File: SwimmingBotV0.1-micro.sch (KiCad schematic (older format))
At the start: 32 parts, among them P11 DEBUG, U8 MAX6034_25, U9 STM32F446-144, X1 CRYSTAL_SMD, Y1 Crystal

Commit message: woohoo getting there
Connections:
- net PB7 is gone; now on net SDA: U9.137 (PB7)
- net PD3 is gone; now on net DCMI_D5: U9.117 (PD3)
- net DCMI_D5: no longer U9.136 (PB6)
- net SCL: now also U9.136 (PB6); no longer U9.69 (PB10)
- net SDA: no longer U9.70 (PB11)
- new net PB10: U9.69 (PB10)
- new net PB11: U9.70 (PB11)
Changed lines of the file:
@@
 $Descr A4 11693 8268
 encoding utf-8
-Sheet 8 8
+Sheet 7 8
 Title ""
 Date ""
@@
 Text HLabel 7050 1300 1    60   Input ~ 0
 DCMI_D4
-Text HLabel 4650 1300 1    60   Input ~ 0
+Text HLabel 6550 1300 1    60   Input ~ 0
 DCMI_D5
 Text HLabel 4350 1300 1    60   Input ~ 0
@@
 Wire Wire Line
 	4050 1350 4050 1300
-Text Label 7050 5800 3    60   ~ 0
+Text Label 4650 1300 1    60   ~ 0
 SCL
-Text Label 7150 5800 3    60   ~ 0
+Text Label 4550 1300 1    60   ~ 0
 SDA
 $Comp
@@
 Text HLabel 6950 1300 1    60   Input ~ 0
 PC12
-Text HLabel 6550 1300 1    60   Input ~ 0
-PD3
+Text HLabel 7150 5800 3    60   Input ~ 0
+PB11
 Text HLabel 5650 1300 1    60   Input ~ 0
 PG11
@@
 Text HLabel 5350 1300 1    60   Input ~ 0
 PG14
-Text HLabel 4550 1300 1    60   Input ~ 0
-PB7
+Text HLabel 7050 5800 3    60   Input ~ 0
+PB10
 $Comp
 L JUMPER JP1

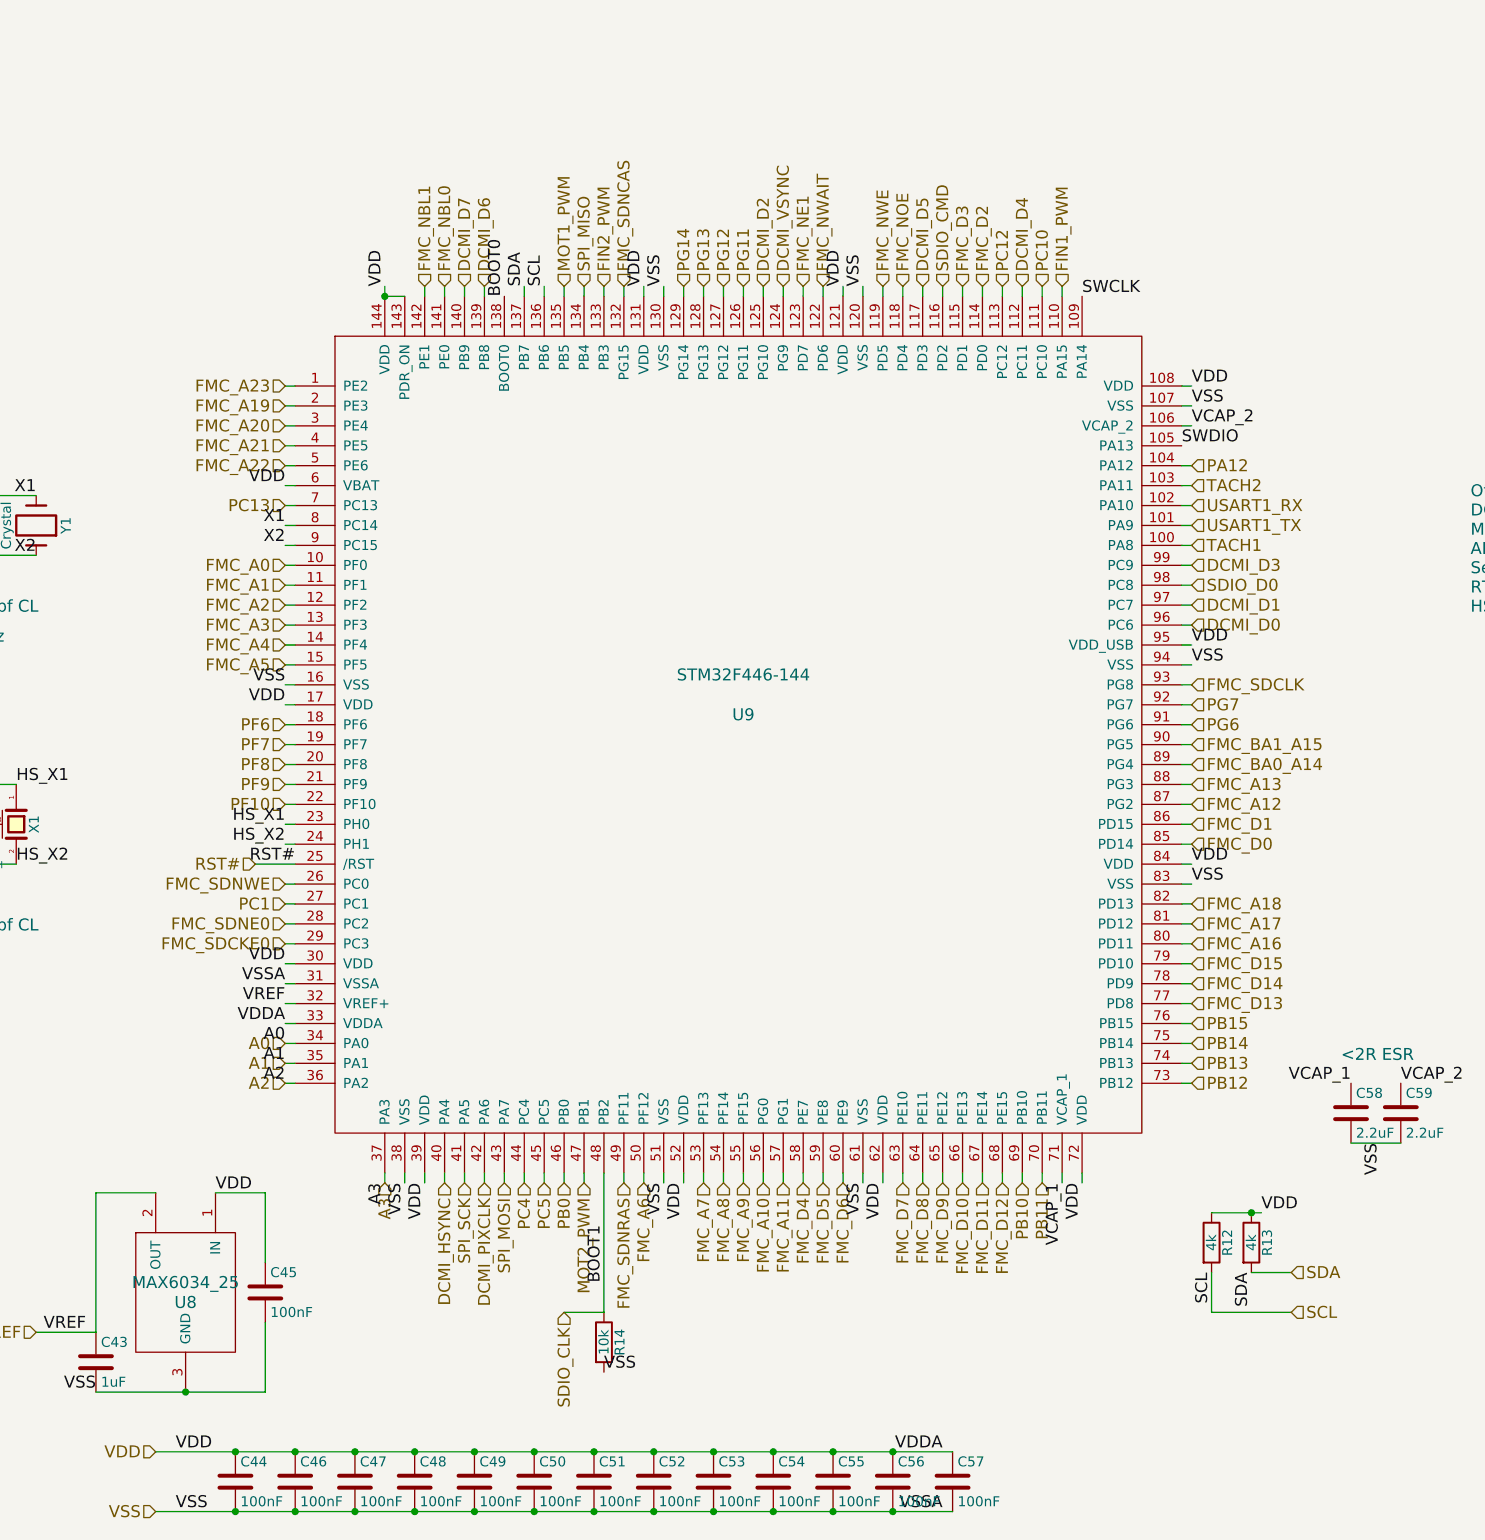
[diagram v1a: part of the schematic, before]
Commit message: removed old ram and flash, added new flash, switched to 100 pin micro
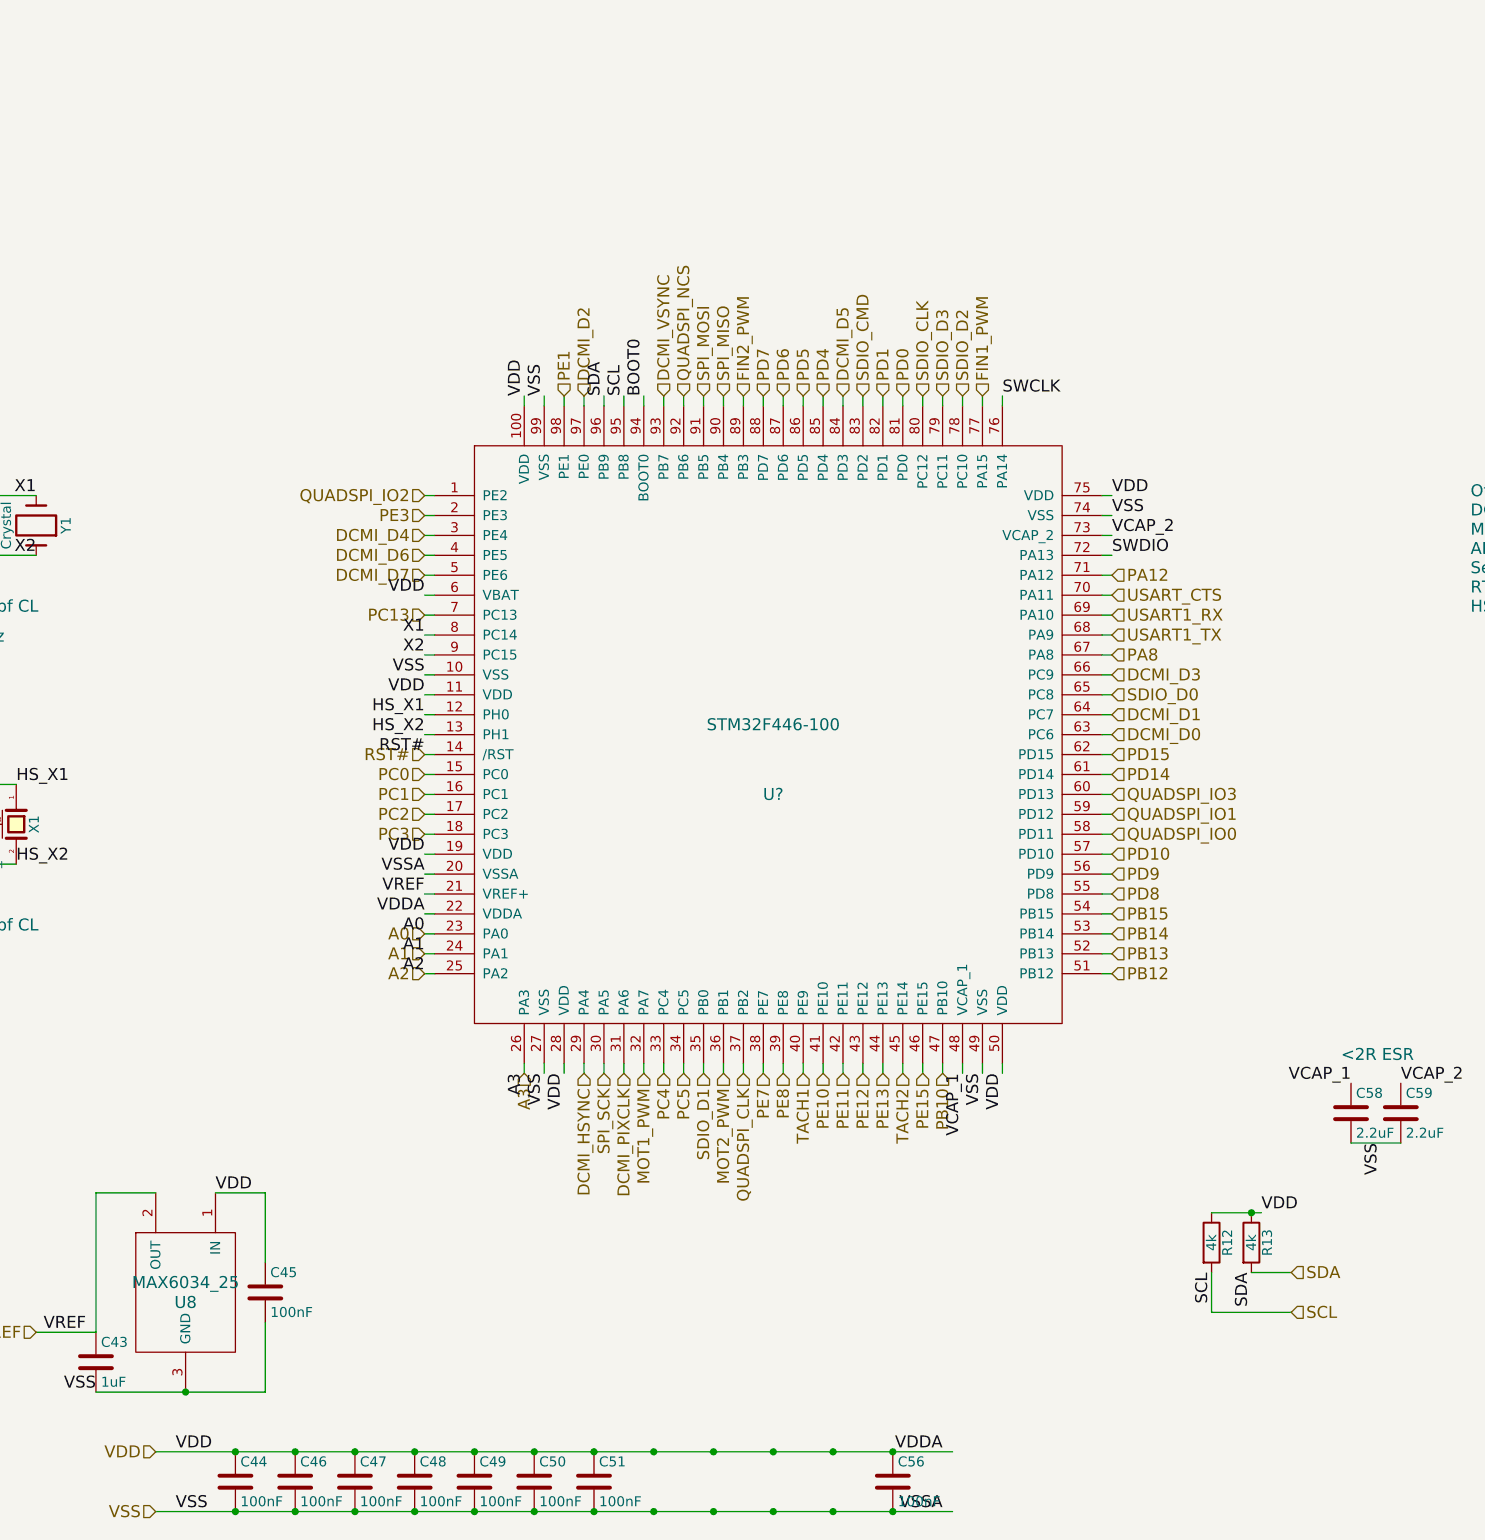
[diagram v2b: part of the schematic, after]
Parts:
- removed C52, C53, C54, C55, C57: 100nF, Capacitors_SMD:C_0402, symbol C
- removed R14: 10k, Resistors_SMD:R_0402, symbol R
- removed U9: STM32F446-144, Housings_QFP:LQFP-144_20x20mm_Pitch0.5mm, symbol STM32F446-144
- added U?: STM32F446-100, symbol STM32F446-100
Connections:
- net A0: now also U?.23 (PA0)
- net A1: now also U?.24 (PA1)
- net A2: now also U?.25 (PA2)
- net A3: now also U?.26 (PA3)
- net BOOT0: now also U?.94 (BOOT0)
- net DCMI_D0: now also U?.63 (PC6)
- net DCMI_D1: now also U?.64 (PC7)
- net DCMI_D2: now also U?.97 (PE0)
- net DCMI_D3: now also U?.66 (PC9)
- net DCMI_D4: now also U?.3 (PE4)
- net DCMI_D5: now also U?.84 (PD3)
- net DCMI_D6: now also U?.4 (PE5)
- net DCMI_D7: now also U?.5 (PE6)
- net DCMI_HSYNC: now also U?.29 (PA4)
- net DCMI_PIXCLK: now also U?.31 (PA6)
- net DCMI_VSYNC: now also U?.93 (PB7)
- net FIN1_PWM: now also U?.77 (PA15)
- net FIN2_PWM: now also U?.89 (PB3)
- net HS_X1: now also U?.12 (PH0)
- net HS_X2: now also U?.13 (PH1)
- net MOT1_PWM: now also U?.32 (PA7)
- net MOT2_PWM: now also U?.36 (PB1)
- net PA12: now also U?.71 (PA12)
- net PB10: now also U?.47 (PB10)
- net PB12: now also U?.51 (PB12)
- net PB13: now also U?.52 (PB13)
- net PB14: now also U?.53 (PB14)
- net PB15: now also U?.54 (PB15)
- net PC1: now also U?.16 (PC1)
- net PC13: now also U?.7 (PC13)
- net PC4: now also U?.33 (PC4)
- net PC5: now also U?.34 (PC5)
- net RST#: now also U?.14 (/RST)
- net SCL: now also U?.95 (PB8)
- net SDA: now also U?.96 (PB9)
- net SDIO_CLK: now also U?.80 (PC12)
- net SDIO_CMD: now also U?.83 (PD2)
- net SDIO_D0: now also U?.65 (PC8)
- net SPI_MISO: now also U?.90 (PB4)
- net SPI_MOSI: now also U?.91 (PB5)
- net SPI_SCK: now also U?.30 (PA5)
- net SWCLK: now also U?.76 (PA14)
- net SWDIO: now also U?.72 (PA13)
- net TACH1: now also U?.40 (PE9)
- net TACH2: now also U?.45 (PE14)
- net USART1_RX: now also U?.69 (PA10)
- net USART1_TX: now also U?.68 (PA9)
- net VCAP_1: now also U?.48 (VCAP_1)
- net VCAP_2: now also U?.73 (VCAP_2)
- net VDD: now also U?.100 (VDD), U?.11 (VDD), U?.19 (VDD), U?.22 (VDDA), U?.28 (VDD), U?.50 (VDD), U?.6 (VBAT), U?.75 (VDD)
- net VREF: now also U?.21 (VREF+)
- net VSS: now also U?.10 (VSS), U?.20 (VSSA), U?.27 (VSS), U?.49 (VSS), U?.74 (VSS), U?.99 (VSS)
- net X1: now also U?.8 (PC14)
- net X2: now also U?.9 (PC15)
- new net PA8: U?.67 (PA8)
- new net PC0: U?.15 (PC0)
- new net PC2: U?.17 (PC2)
- new net PC3: U?.18 (PC3)
- new net PD0: U?.81 (PD0)
- new net PD1: U?.82 (PD1)
- new net PD10: U?.57 (PD10)
- new net PD14: U?.61 (PD14)
- new net PD15: U?.62 (PD15)
- new net PD4: U?.85 (PD4)
- new net PD5: U?.86 (PD5)
- new net PD6: U?.87 (PD6)
- new net PD7: U?.88 (PD7)
- new net PD8: U?.55 (PD8)
- new net PD9: U?.56 (PD9)
- new net PE1: U?.98 (PE1)
- new net PE10: U?.41 (PE10)
- new net PE11: U?.42 (PE11)
- new net PE12: U?.43 (PE12)
- new net PE13: U?.44 (PE13)
- new net PE15: U?.46 (PE15)
- new net PE3: U?.2 (PE3)
- new net PE7: U?.38 (PE7)
- new net PE8: U?.39 (PE8)
- new net QUADSPI_CLK: U?.37 (PB2)
- new net QUADSPI_IO0: U?.58 (PD11)
- new net QUADSPI_IO1: U?.59 (PD12)
- new net QUADSPI_IO2: U?.1 (PE2)
- new net QUADSPI_IO3: U?.60 (PD13)
- new net QUADSPI_NCS: U?.92 (PB6)
- new net SDIO_D1: U?.35 (PB0)
- new net SDIO_D2: U?.78 (PC10)
- new net SDIO_D3: U?.79 (PC11)
- new net USART_CTS: U?.70 (PA11)

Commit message: potentially done with parts removal and reselection, on to pcb layout
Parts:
- gave numbers to parts that had none: 1
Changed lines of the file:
@@
 $EndComp
 $Comp
-L STM32F446-100 U?
+L STM32F446-100 U12
 U 1 1 57935929
 P 5800 3750
-F 0 "U?" H 5800 3650 60  0000 C CNN
+F 0 "U12" H 5800 3650 60  0000 C CNN
 F 1 "STM32F446-100" H 5800 4000 60  0000 C CNN
 F 2 "" H 5200 5150 60  0000 C CNN

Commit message: pcb started in earnest, footprint changes in schematics, about to rename v0.2 boardfile to v0.1, kicad needs the same filename to have backrefs for net highlighting
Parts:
- JP1: footprint Custom_Footprints:JUMPER -> Oddities:NetTie-I_Connected_SMD
- U12: footprint (none) -> Custom_Footprints:STM32F446_QFP_100
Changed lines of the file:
@@
 F 0 "JP1" H 9900 4500 50  0000 C CNN
 F 1 "JUMPER" H 9900 4270 50  0000 C CNN
-F 2 "Custom_Footprints:JUMPER" H 9900 4350 50  0001 C CNN
+F 2 "Oddities:NetTie-I_Connected_SMD" H 9900 4350 50  0001 C CNN
 F 3 "" H 9900 4350 50  0000 C CNN
 	1    9900 4350
@@
 F 0 "U12" H 5800 3650 60  0000 C CNN
 F 1 "STM32F446-100" H 5800 4000 60  0000 C CNN
-F 2 "" H 5200 5150 60  0000 C CNN
+F 2 "Custom_Footprints:STM32F446_QFP_100" H 5200 5150 60  0001 C CNN
 F 3 "" H 5200 5150 60  0000 C CNN
 	1    5800 3750

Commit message: different solder bridge, done with routing, moving silk layer around now
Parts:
- JP1: footprint Oddities:NetTie-I_Connected_SMD -> Custom_Footprints:SOLDER-JUMPER
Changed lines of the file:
@@
 F 0 "JP1" H 9900 4500 50  0000 C CNN
 F 1 "JUMPER" H 9900 4270 50  0000 C CNN
-F 2 "Oddities:NetTie-I_Connected_SMD" H 9900 4350 50  0001 C CNN
+F 2 "Custom_Footprints:SOLDER-JUMPER" H 9900 4350 50  0001 C CNN
 F 3 "" H 9900 4350 50  0000 C CNN
 	1    9900 4350

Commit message: submitted to fab woohoo
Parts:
- JP1: value JUMPER -> BOOT0
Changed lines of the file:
@@
 P 9900 4350
 F 0 "JP1" H 9900 4500 50  0000 C CNN
-F 1 "JUMPER" H 9900 4270 50  0000 C CNN
+F 1 "BOOT0" H 9900 4270 50  0000 C CNN
 F 2 "Custom_Footprints:SOLDER-JUMPER" H 9900 4350 50  0001 C CNN
 F 3 "" H 9900 4350 50  0000 C CNN
